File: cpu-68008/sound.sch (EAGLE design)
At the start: 59 parts, among them IC101 GAL22V10D, IC102 74HCT175N, IC201 YM3812, IC202 YM3014B, IC203 AY-3-8910, IC301 TL062, IC302 TL062, IC401 74HCT14N, IC402 TL16C550D, J301 RCALOCK, J401 DIN5, J402 DIN5

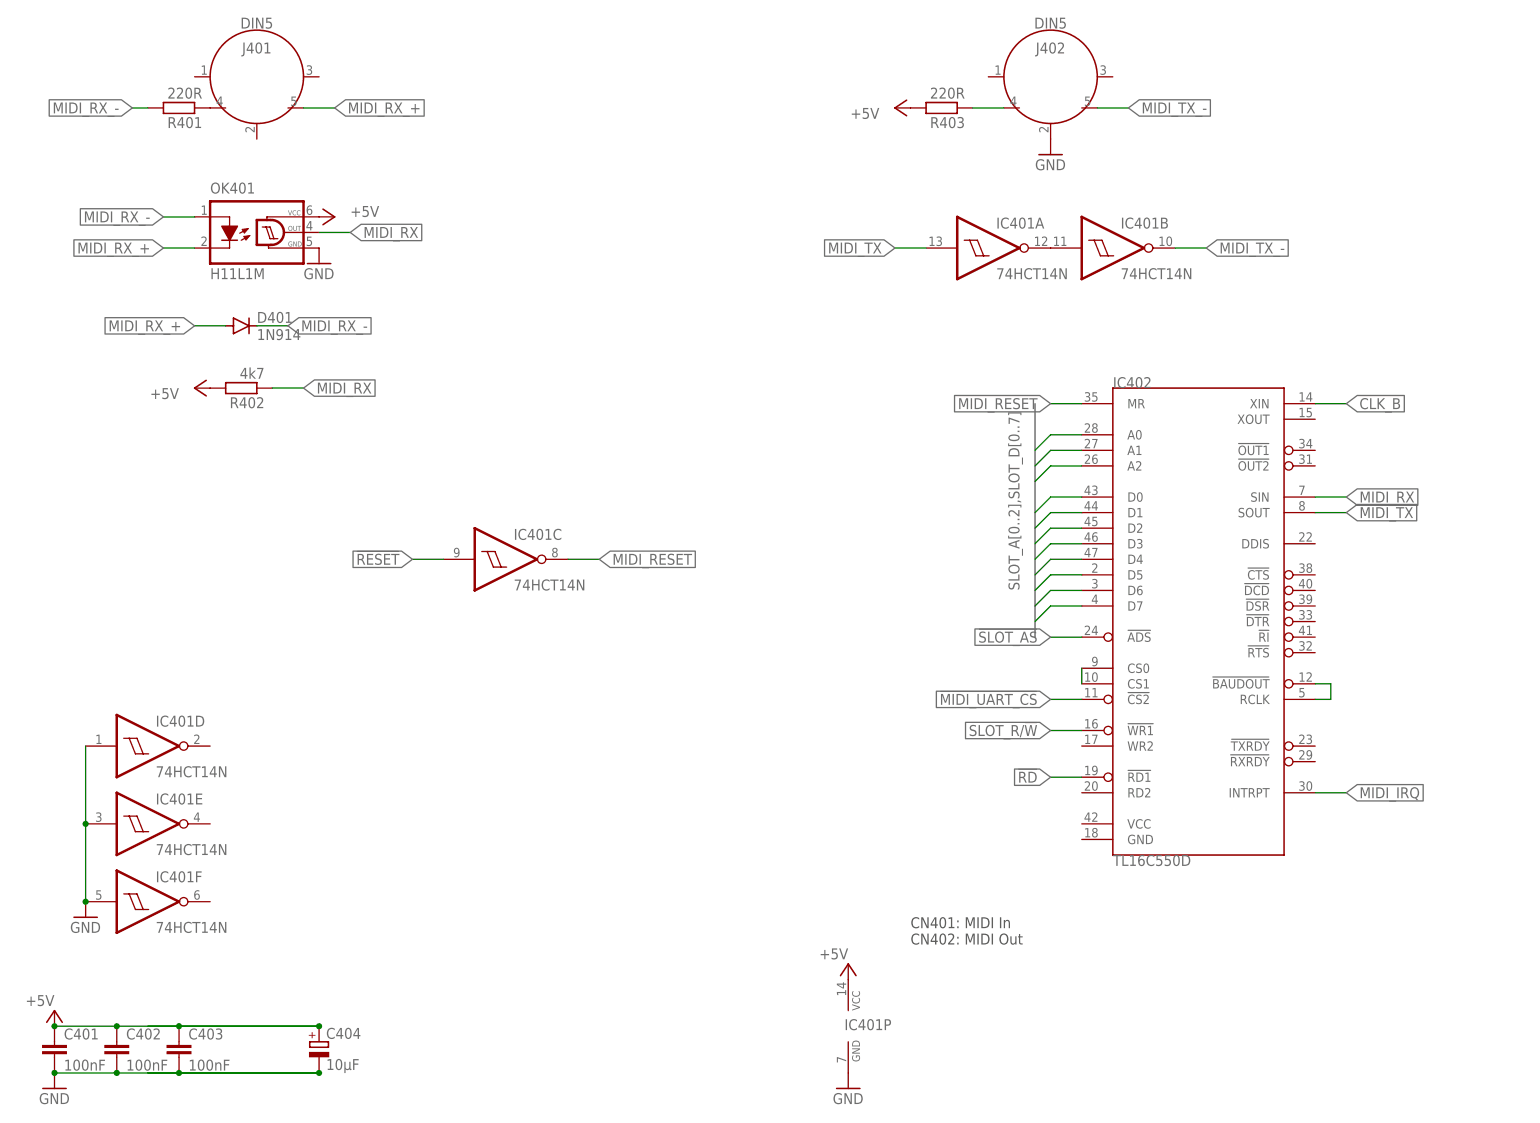
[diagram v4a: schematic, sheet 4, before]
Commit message: finished routing sound board; added correct CPU board PLDs
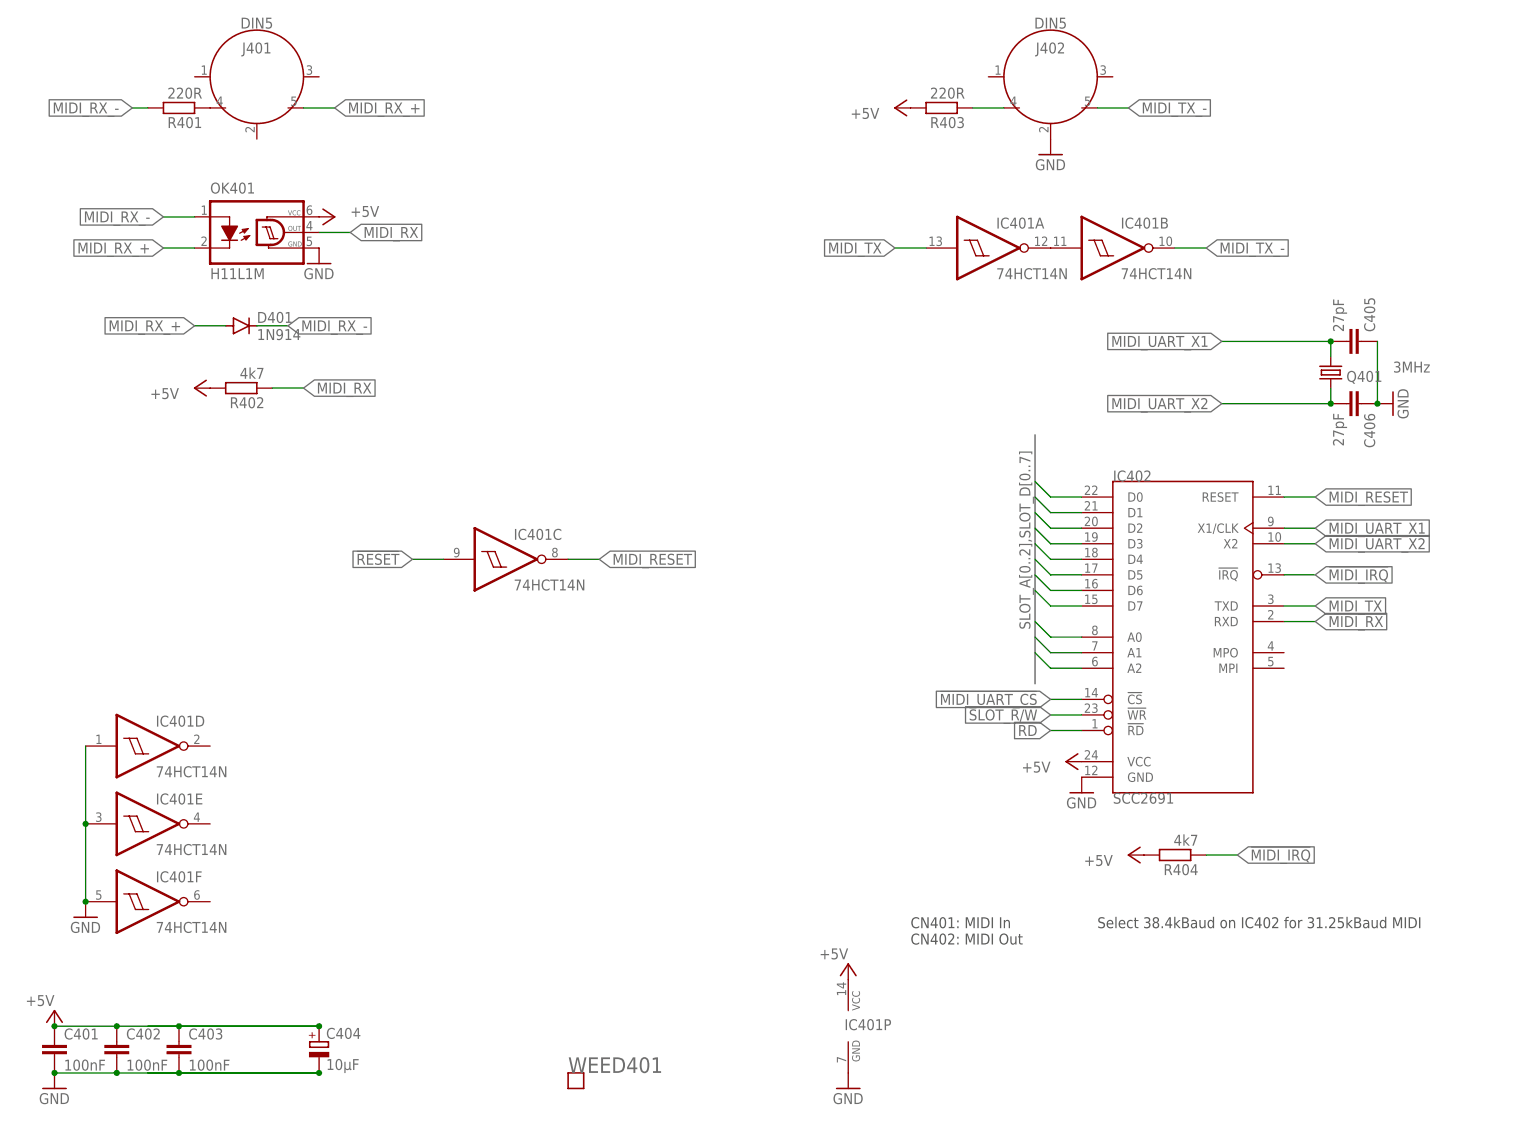
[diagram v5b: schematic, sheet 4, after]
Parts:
- removed C206: 10µF, rcl:CPOL-EUSMCB
- removed QG202: (no value), crystal:XO-8
- added C405, C406: 27pF, rcl:C-EUC0805
- added Q401: 3MHz, crystal:CRYSTALHC49S
- added R404: 4k7, rcl:R-EU_R2012
- added WEED401: WEED, 68komputer:WEED
- C205: value 100nF -> 10µF; device rcl:C-EUC0805 -> rcl:CPOL-EUSMCB; MOUSER 710-885012207072 -> 581-TAJB106K020RNJV
- IC402: value TL16C550D -> SCC2691; device 68komputer:TL16C550DLQFP-48 -> 68komputer:SCC2691
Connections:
- removed net CLK_B: IC203.CLK, IC402.XIN, QG202.OUT
- removed net MIDI_IRQ: IC101.IN9, IC402.INTRPT
- removed net N$3: IC402.!BAUDOUT, IC402.RCLK
- removed net N$8: IC402.CS0, IC402.CS1
- new net !MIDI_IRQ: IC101.IN9, IC402.!IRQ, R404.1
- new net MIDI_UART_X1: C405.2, IC402.X1/CLK, Q401.1
- new net MIDI_UART_X2: C406.2, IC402.X2, Q401.2
- net !MIDI_UART_CS: now also IC402.!CS; no longer IC402.!CS2
- net !RD: now also IC402.!RD; no longer IC402.!RD1
- net !SLOT_AS: no longer IC402.!ADS
- net +5V: now also C205.+, IC402.VCC, R404.2; no longer C205.1, C206.+, QG202.VCC
- net CLK_A: now also IC203.CLK
- net GND: now also C205.-, C405.1, C406.1, IC402.GND; no longer C205.2, C206.-, QG202.GND
- net MIDI_RESET: now also IC402.RESET; no longer IC402.MR
- net MIDI_RX: now also IC402.RXD; no longer IC402.SIN
- net MIDI_TX: now also IC402.TXD; no longer IC402.SOUT
- net SLOT_R/!W!: now also IC402.!WR; no longer IC402.!WR1
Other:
- note added: "Select 38.4kBaud on IC402 for 31.25kBaud MIDI"
- moved on the sheet: C202, C203, C204
